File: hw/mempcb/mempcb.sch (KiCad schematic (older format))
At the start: 32 parts, among them J1 RC6502_Bus, J2 0.1\" 2x25, U3 JEDEC_DIP32_RAM, U4 74LS138, U5 74LS138

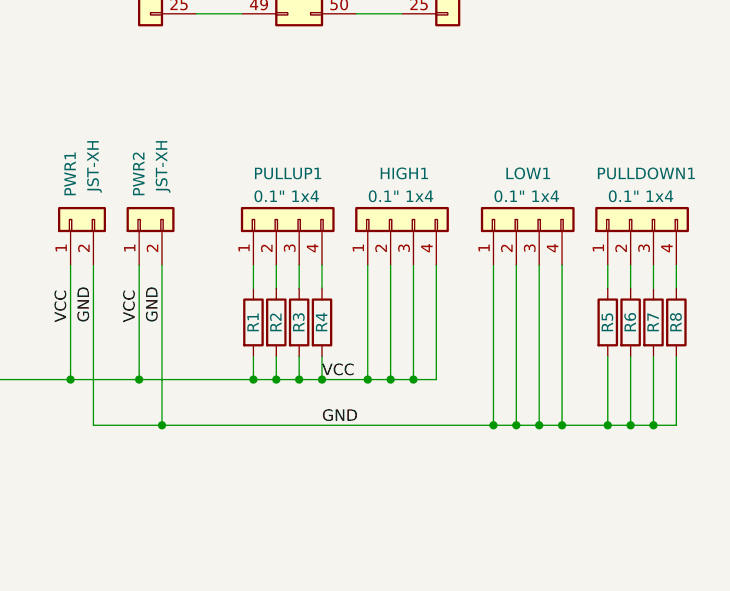
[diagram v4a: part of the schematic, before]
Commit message: hw/mempcb/: Use just 4 pins instead of 8 for spare GND/Vcc
These don't need to be separate for each circuit, as the pullups do.
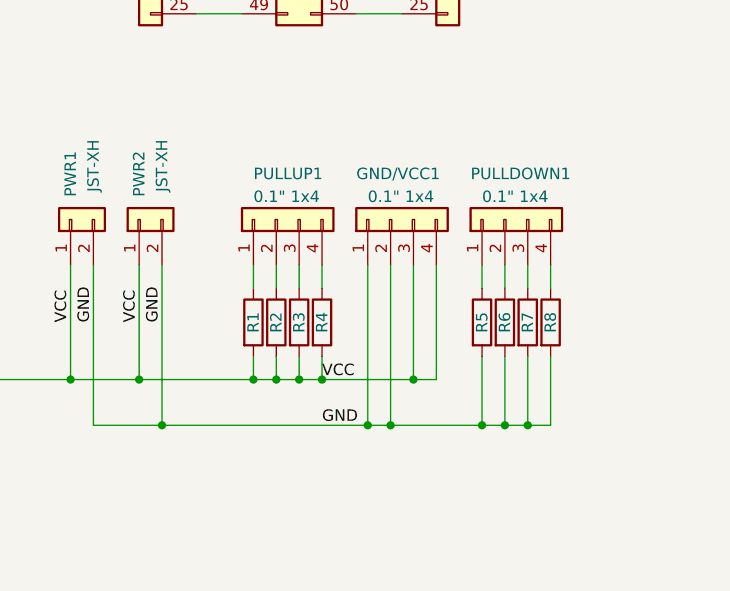
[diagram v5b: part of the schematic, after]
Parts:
- removed LOW1: 0.1\" 1x4, Connector_PinHeader_2.54mm:PinHeader_1x04_P2.54mm_Vertical, symbol Connector_Generic:Conn_01x04
- renumbered HIGH1 to GND/VCC1
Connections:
- net GND: now also GND/VCC1.1 (Pin_1), GND/VCC1.2 (Pin_2)
- net VCC: no longer GND/VCC1.1 (Pin_1), GND/VCC1.2 (Pin_2)
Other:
- moved on the sheet: PULLDOWN1, R5, R6, R7, R8
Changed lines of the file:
@@
 VCC
 $Comp
-L Connector_Generic:Conn_01x04 HIGH1
+L Connector_Generic:Conn_01x04 GND/VCC1
 U 1 1 5FED18C8
 P 9300 4850
-F 0 "HIGH1" V 9500 4900 50  0000 R CNN
+F 0 "GND/VCC1" V 9500 5000 50  0000 R CNN
 F 1 "0.1\" 1x4" V 9400 4950 50  0000 R CNN
 F 2 "Connector_PinHeader_2.54mm:PinHeader_1x04_P2.54mm_Vertical" H 9300 4850 50  0001 C CNN
 F 3 "~" H 9300 4850 50  0001 C CNN
 	1    9300 4850
-	0    -1   -1   0
-$EndComp
-$Comp
-L Connector_Generic:Conn_01x04 LOW1
-U 1 1 603235A5
-P 9850 4850
-F 0 "LOW1" V 10050 4900 50  0000 R CNN
-F 1 "0.1\" 1x4" V 9950 4950 50  0000 R CNN
-F 2 "Connector_PinHeader_2.54mm:PinHeader_1x04_P2.54mm_Vertical" H 9850 4850 50  0001 C CNN
-F 3 "~" H 9850 4850 50  0001 C CNN
-	1    9850 4850
 	0    -1   -1   0
 $EndComp
@@
 L Connector_Generic:Conn_01x04 PULLDOWN1
 U 1 1 6042687B
-P 10350 4850
-F 0 "PULLDOWN1" V 10550 5000 50  0000 R CNN
-F 1 "0.1\" 1x4" V 10450 4950 50  0000 R CNN
-F 2 "Connector_PinHeader_2.54mm:PinHeader_1x04_P2.54mm_Vertical" H 10350 4850 50  0001 C CNN
-F 3 "~" H 10350 4850 50  0001 C CNN
-	1    10350 4850
+P 9800 4850
+F 0 "PULLDOWN1" V 10000 5000 50  0000 R CNN
+F 1 "0.1\" 1x4" V 9900 4950 50  0000 R CNN
+F 2 "Connector_PinHeader_2.54mm:PinHeader_1x04_P2.54mm_Vertical" H 9800 4850 50  0001 C CNN
+F 3 "~" H 9800 4850 50  0001 C CNN
+	1    9800 4850
 	0    -1   -1   0
 $EndComp
@@
 L Device:R R5
 U 1 1 60426881
-P 10250 5300
-F 0 "R5" V 10250 5300 50  0000 C CNN
-F 1 "R" V 10250 5300 50  0001 C CNN
-F 2 "Resistor_THT:R_Axial_DIN0207_L6.3mm_D2.5mm_P10.16mm_Horizontal" V 10180 5300 50  0001 C CNN
-F 3 "~" H 10250 5300 50  0001 C CNN
-	1    10250 5300
-	1    0    0    -1
-$EndComp
-Wire Wire Line
-	10250 5150 10250 5050
+P 9700 5300
+F 0 "R5" V 9700 5300 50  0000 C CNN
+F 1 "R" V 9700 5300 50  0001 C CNN
+F 2 "Resistor_THT:R_Axial_DIN0207_L6.3mm_D2.5mm_P10.16mm_Horizontal" V 9630 5300 50  0001 C CNN
+F 3 "~" H 9700 5300 50  0001 C CNN
+	1    9700 5300
+	1    0    0    -1
+$EndComp
+Wire Wire Line
+	9700 5150 9700 5050
 $Comp
 L Device:R R6
 U 1 1 60426889
-P 10350 5300
-F 0 "R6" V 10350 5300 50  0000 C CNN
-F 1 "R" V 10350 5300 50  0001 C CNN
-F 2 "Resistor_THT:R_Axial_DIN0207_L6.3mm_D2.5mm_P10.16mm_Horizontal" V 10280 5300 50  0001 C CNN
-F 3 "~" H 10350 5300 50  0001 C CNN
-	1    10350 5300
-	1    0    0    -1
-$EndComp
-Wire Wire Line
-	10350 5150 10350 5050
+P 9800 5300
+F 0 "R6" V 9800 5300 50  0000 C CNN
+F 1 "R" V 9800 5300 50  0001 C CNN
+F 2 "Resistor_THT:R_Axial_DIN0207_L6.3mm_D2.5mm_P10.16mm_Horizontal" V 9730 5300 50  0001 C CNN
+F 3 "~" H 9800 5300 50  0001 C CNN
+	1    9800 5300
+	1    0    0    -1
+$EndComp
+Wire Wire Line
+	9800 5150 9800 5050
 $Comp
 L Device:R R7
 U 1 1 60426891
-P 10450 5300
-F 0 "R7" V 10450 5300 50  0000 C CNN
-F 1 "R" V 10450 5300 50  0001 C CNN
-F 2 "Resistor_THT:R_Axial_DIN0207_L6.3mm_D2.5mm_P10.16mm_Horizontal" V 10380 5300 50  0001 C CNN
-F 3 "~" H 10450 5300 50  0001 C CNN
-	1    10450 5300
-	1    0    0    -1
-$EndComp
-Wire Wire Line
-	10450 5150 10450 5050
+P 9900 5300
+F 0 "R7" V 9900 5300 50  0000 C CNN
+F 1 "R" V 9900 5300 50  0001 C CNN
+F 2 "Resistor_THT:R_Axial_DIN0207_L6.3mm_D2.5mm_P10.16mm_Horizontal" V 9830 5300 50  0001 C CNN
+F 3 "~" H 9900 5300 50  0001 C CNN
+	1    9900 5300
+	1    0    0    -1
+$EndComp
+Wire Wire Line
+	9900 5150 9900 5050
 $Comp
 L Device:R R8
 U 1 1 60426899
-P 10550 5300
-F 0 "R8" V 10550 5300 50  0000 C CNN
-F 1 "R" V 10550 5300 50  0001 C CNN
-F 2 "Resistor_THT:R_Axial_DIN0207_L6.3mm_D2.5mm_P10.16mm_Horizontal" V 10480 5300 50  0001 C CNN
-F 3 "~" H 10550 5300 50  0001 C CNN
-	1    10550 5300
-	1    0    0    -1
-$EndComp
-Wire Wire Line
-	10550 5150 10550 5050
-Wire Wire Line
-	9000 5550 9200 5550
-Wire Wire Line
-	9500 5050 9500 5550
+P 10000 5300
+F 0 "R8" V 10000 5300 50  0000 C CNN
+F 1 "R" V 10000 5300 50  0001 C CNN
+F 2 "Resistor_THT:R_Axial_DIN0207_L6.3mm_D2.5mm_P10.16mm_Horizontal" V 9930 5300 50  0001 C CNN
+F 3 "~" H 10000 5300 50  0001 C CNN
+	1    10000 5300
+	1    0    0    -1
+$EndComp
+Wire Wire Line
+	10000 5150 10000 5050
 Connection ~ 9000 5550
-Wire Wire Line
-	9400 5050 9400 5550
-Connection ~ 9400 5550
-Wire Wire Line
-	9400 5550 9500 5550
-Wire Wire Line
-	9300 5050 9300 5550
-Connection ~ 9300 5550
-Wire Wire Line
-	9300 5550 9400 5550
-Wire Wire Line
-	9200 5050 9200 5550
-Connection ~ 9200 5550
-Wire Wire Line
-	9200 5550 9300 5550
 Text Label 9000 5550 0    50   ~ 0
 VCC
@@
 Connection ~ 8300 5750
 Wire Wire Line
-	8300 5750 9750 5750
-Wire Wire Line
-	10550 5450 10550 5750
-Wire Wire Line
-	10450 5450 10450 5750
-Connection ~ 10450 5750
-Wire Wire Line
-	10450 5750 10550 5750
-Wire Wire Line
-	10350 5450 10350 5750
-Connection ~ 10350 5750
-Wire Wire Line
-	10350 5750 10450 5750
-Wire Wire Line
-	10250 5450 10250 5750
-Connection ~ 10250 5750
-Wire Wire Line
-	10250 5750 10350 5750
-Wire Wire Line
-	10050 5050 10050 5750
-Connection ~ 10050 5750
-Wire Wire Line
-	10050 5750 10250 5750
-Wire Wire Line
-	9950 5050 9950 5750
-Connection ~ 9950 5750
-Wire Wire Line
-	9950 5750 10050 5750
-Wire Wire Line
-	9850 5050 9850 5750
-Connection ~ 9850 5750
-Wire Wire Line
-	9850 5750 9950 5750
-Wire Wire Line
-	9750 5050 9750 5750
-Connection ~ 9750 5750
-Wire Wire Line
-	9750 5750 9850 5750
+	10000 5450 10000 5750
+Wire Wire Line
+	9900 5450 9900 5750
+Connection ~ 9900 5750
+Wire Wire Line
+	9900 5750 10000 5750
+Wire Wire Line
+	9800 5450 9800 5750
+Connection ~ 9800 5750
+Wire Wire Line
+	9800 5750 9900 5750
+Wire Wire Line
+	9700 5450 9700 5750
+Wire Wire Line
+	9700 5750 9800 5750
 Text Label 9000 5750 0    50   ~ 0
 GND
@@
 	0    1    1    0
 $EndComp
+Wire Wire Line
+	8300 5750 9200 5750
+Wire Wire Line
+	9500 5550 9500 5050
+Wire Wire Line
+	9000 5550 9400 5550
+Wire Wire Line
+	9400 5050 9400 5550
+Connection ~ 9400 5550
+Wire Wire Line
+	9400 5550 9500 5550
+Wire Wire Line
+	9200 5050 9200 5750
+Connection ~ 9200 5750
+Wire Wire Line
+	9200 5750 9300 5750
+Wire Wire Line
+	9300 5050 9300 5750
+Wire Wire Line
+	9700 5750 9300 5750
+Connection ~ 9700 5750
+Connection ~ 9300 5750
 $EndSCHEMATC

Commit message: hw/mempcb/: Update ZIF socket footprint in layout
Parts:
- U3: footprint Package_DIP:DIP-32_W15.24mm_Socket_LongPads -> mempcb:DIP-32_W15.24mm_ZIF_Socket_LongPads
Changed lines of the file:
@@
 F 0 "U3" H 5500 3267 50  0000 C CNN
 F 1 "JEDEC_DIP32_RAM" H 5500 3176 50  0000 C CNN
-F 2 "Package_DIP:DIP-32_W15.24mm_Socket_LongPads" H 5500 2100 50  0001 C CNN
+F 2 "mempcb:DIP-32_W15.24mm_ZIF_Socket_LongPads" H 5500 2100 50  0001 C CNN
 F 3 "http://www.futurlec.com/Datasheet/Memory/628128.pdf" H 5500 2100 50  0001 C CNN
 	1    5500 2100

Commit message: hw/mempcb: Move all parts on to a .05"/1.27mm grid
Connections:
- net A7: now also U3.5 (A7), W3_1.5 (Pin_5)
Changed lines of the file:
@@
 Connection ~ 9700 5750
 Connection ~ 9300 5750
+Text Label 4750 1700 0    50   ~ 0
+A7
 $EndSCHEMATC

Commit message: hw/mempcb sch: Save automatic changes from my first opening of this
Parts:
- BUSPWR_EN1, PWR1, PWR2: symbol Connector_Generic:Conn_01x02 -> mempcb-rescue:Conn_01x02-Connector_Generic
- C1, C2, C3: symbol Device:C -> mempcb-rescue:C-Device
- GND/VCC1, PULLDOWN1, PULLUP1: symbol Connector_Generic:Conn_01x04 -> mempcb-rescue:Conn_01x04-Connector_Generic
- J2: symbol Connector_Generic:Conn_02x25_Odd_Even -> mempcb-rescue:Conn_02x25_Odd_Even-Connector_Generic
- R1, R2, R3, R4, R5, R6, R7, R8: symbol Device:R -> mempcb-rescue:R-Device
- W2_1, W2_2: symbol Connector_Generic:Conn_01x25 -> mempcb-rescue:Conn_01x25-Connector_Generic
- W3_1, W3_2: symbol Connector_Generic:Conn_01x16 -> mempcb-rescue:Conn_01x16-Connector_Generic
- W4_1, W4_2, W5_1, W5_2: symbol Connector_Generic:Conn_01x08 -> mempcb-rescue:Conn_01x08-Connector_Generic
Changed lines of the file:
@@
 EESchema Schematic File Version 4
-EELAYER 30 0
+LIBS:mempcb-cache
+EELAYER 26 0
 EELAYER END
 $Descr A4 11693 8268
@@
 $EndComp
 $Comp
-L Connector_Generic:Conn_02x25_Odd_Even J2
+L mempcb-rescue:Conn_02x25_Odd_Even-Connector_Generic J2
 U 1 1 5FEB0496
 P 8850 2750
@@
 $EndComp
 $Comp
-L Connector_Generic:Conn_01x25 W2_1
+L mempcb-rescue:Conn_01x25-Connector_Generic W2_1
 U 1 1 5FEB2EF1
 P 8250 2750
@@
 $EndComp
 $Comp
-L Connector_Generic:Conn_01x25 W2_2
+L mempcb-rescue:Conn_01x25-Connector_Generic W2_2
 U 1 1 5FEC1F3E
 P 9550 2750
@@
 $EndComp
 $Comp
-L Connector_Generic:Conn_01x16 W3_1
+L mempcb-rescue:Conn_01x16-Connector_Generic W3_1
 U 1 1 5FECEA90
 P 4550 2000
@@
 $EndComp
 $Comp
-L Connector_Generic:Conn_01x08 W4_2
+L mempcb-rescue:Conn_01x08-Connector_Generic W4_2
 U 1 1 5FECFD2E
 P 6500 4150
@@
 $EndComp
 $Comp
-L Connector_Generic:Conn_01x08 W4_1
+L mempcb-rescue:Conn_01x08-Connector_Generic W4_1
 U 1 1 5FED086C
 P 4500 4150
@@
 	6250 1300 6200 1300
 $Comp
-L Connector_Generic:Conn_01x16 W3_2
+L mempcb-rescue:Conn_01x16-Connector_Generic W3_2
 U 1 1 5FECF06C
 P 6450 2000
@@
 VCC
 $Comp
-L Connector_Generic:Conn_01x04 GND/VCC1
+L mempcb-rescue:Conn_01x04-Connector_Generic GND/VCC1
 U 1 1 5FED18C8
 P 9300 4850
@@
 $EndComp
 $Comp
-L Connector_Generic:Conn_01x04 PULLUP1
+L mempcb-rescue:Conn_01x04-Connector_Generic PULLUP1
 U 1 1 6032F1DA
 P 8800 4850
@@
 	8700 5150 8700 5050
 $Comp
-L Device:R R2
+L mempcb-rescue:R-Device R2
 U 1 1 603E796E
 P 8800 5300
@@
 	8800 5150 8800 5050
 $Comp
-L Device:R R3
+L mempcb-rescue:R-Device R3
 U 1 1 60400026
 P 8900 5300
@@
 	8900 5150 8900 5050
 $Comp
-L Device:R R4
+L mempcb-rescue:R-Device R4
 U 1 1 6040C3DC
 P 9000 5300
@@
 	8900 5550 9000 5550
 $Comp
-L Connector_Generic:Conn_01x04 PULLDOWN1
+L mempcb-rescue:Conn_01x04-Connector_Generic PULLDOWN1
 U 1 1 6042687B
 P 9800 4850
@@
 $EndComp
 $Comp
-L Device:R R5
+L mempcb-rescue:R-Device R5
 U 1 1 60426881
 P 9700 5300
@@
 	9700 5150 9700 5050
 $Comp
-L Device:R R6
+L mempcb-rescue:R-Device R6
 U 1 1 60426889
 P 9800 5300
@@
 	9800 5150 9800 5050
 $Comp
-L Device:R R7
+L mempcb-rescue:R-Device R7
 U 1 1 60426891
 P 9900 5300
@@
 	9900 5150 9900 5050
 $Comp
-L Device:R R8
+L mempcb-rescue:R-Device R8
 U 1 1 60426899
 P 10000 5300
@@
 VCC
 $Comp
-L Device:R R1
+L mempcb-rescue:R-Device R1
 U 1 1 603CD90C
 P 8700 5300
@@
 $EndComp
 $Comp
-L Connector_Generic:Conn_01x02 PWR1
+L mempcb-rescue:Conn_01x02-Connector_Generic PWR1
 U 1 1 604FEFCF
 P 7900 4850
@@
 GND
 $Comp
-L Connector_Generic:Conn_01x02 PWR2
+L mempcb-rescue:Conn_01x02-Connector_Generic PWR2
 U 1 1 6051B38D
 P 8200 4850
@@
 BUS_VCC
 $Comp
-L Connector_Generic:Conn_01x02 BUSPWR_EN1
+L mempcb-rescue:Conn_01x02-Connector_Generic BUSPWR_EN1
 U 1 1 60556D43
 P 7350 4850
@@
 	6050 3850 6300 3850
 $Comp
-L Device:C C2
+L mempcb-rescue:C-Device C2
 U 1 1 5FF0AFCA
 P 5500 5000
@@
 $EndComp
 $Comp
-L Device:C C1
+L mempcb-rescue:C-Device C1
 U 1 1 5FF2C1A0
 P 5500 3200
@@
 	6200 1300 6000 1300
 $Comp
-L Connector_Generic:Conn_01x08 W5_2
+L mempcb-rescue:Conn_01x08-Connector_Generic W5_2
 U 1 1 5FF51E6E
 P 6500 5800
@@
 $EndComp
 $Comp
-L Connector_Generic:Conn_01x08 W5_1
+L mempcb-rescue:Conn_01x08-Connector_Generic W5_1
 U 1 1 5FF51E74
 P 4500 5800
@@
 	6050 5500 6300 5500
 $Comp
-L Device:C C3
+L mempcb-rescue:C-Device C3
 U 1 1 5FF51E9A
 P 5500 6650
